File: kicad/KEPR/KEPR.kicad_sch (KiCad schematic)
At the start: 0 parts

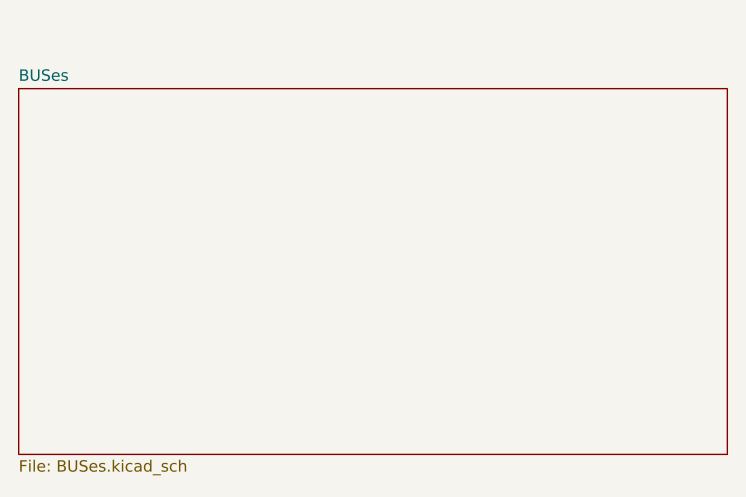
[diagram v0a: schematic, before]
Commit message: Definido os demais buses, criado folha do carimbo, versão 0.5
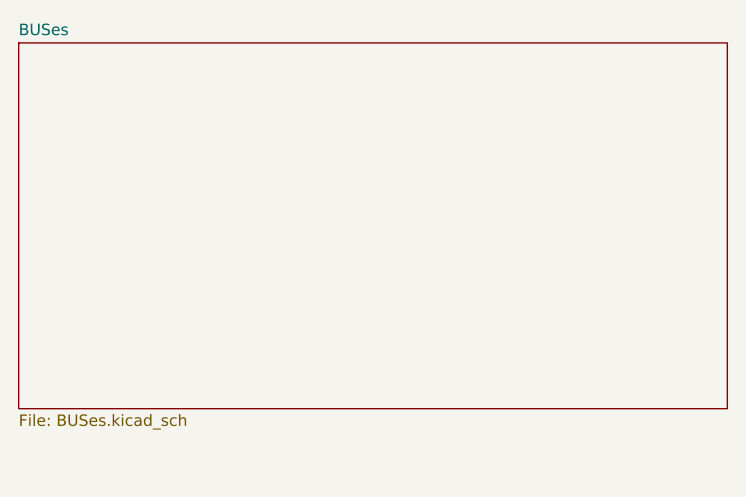
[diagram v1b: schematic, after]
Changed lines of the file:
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@@
 	)
 	(sheet
-		(at 30.48 25.4)
+		(at 30.48 20.32)
 		(size 78.74 40.64)
 		(exclude_from_sim no)
@@
 		)
 		(fill
-			(color 0 0 0 0.0000)
+			(color 255 97 121 1.0000)
 		)
 		(property "Sheetname" "BUSes"
-			(at 30.48 24.6884 0)
+			(at 30.48 19.6084 0)
 			(effects
 				(font
@@
 		)
 		(property "Sheetfile" "BUSes.kicad_sch"
-			(at 30.48 66.6246 0)
+			(at 30.48 61.5446 0)
 			(effects
 				(font
@@
 			(project "KEPR"
 				(path "/5d9e1dfb-5ec5-4e06-bbdb-9cbfa1c0b9f1"
-					(page "5")
+					(page "A001")
 				)
 			)

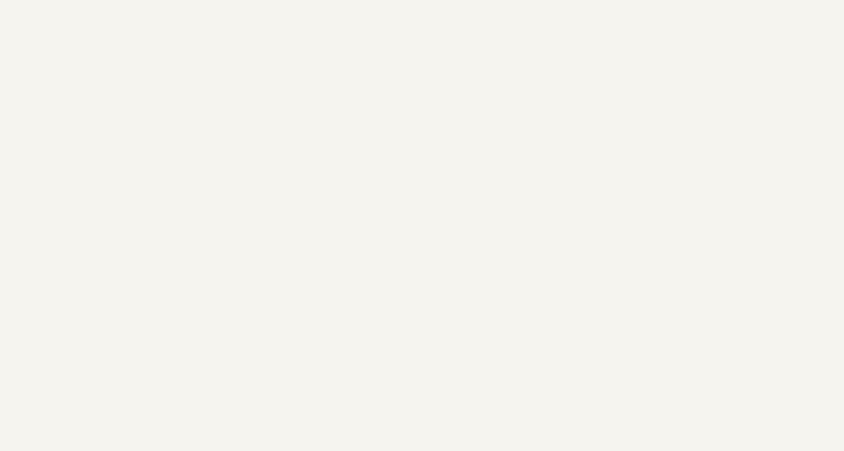
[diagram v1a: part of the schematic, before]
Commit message: Vários ajuste, sendo o mais importante a adição do power rail e iniciado o Wireless module
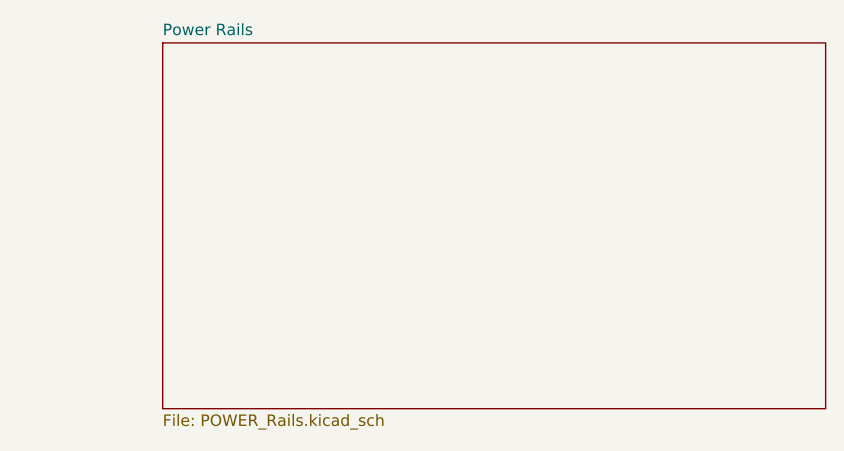
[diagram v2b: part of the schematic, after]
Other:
- added sheet Power Rails (POWER_Rails.kicad_sch)

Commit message: Diversos ajustes no Power Rail
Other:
- sheet Power Rails renamed Power
- added sheet UCE board (UCE_board.kicad_sch)
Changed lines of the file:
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@@
 			(color 0 0 0 0.0000)
 		)
-		(property "Sheetname" "Power Rails"
+		(property "Sheetname" "Power"
 			(at 137.16 19.6084 0)
 			(effects
@@
 			(project "KEPR"
 				(path "/5d9e1dfb-5ec5-4e06-bbdb-9cbfa1c0b9f1"
-					(page "A001")
+					(page "A002")
 				)
 			)
+		)
+	)
+	(sheet
+		(at 238.76 20.32)
+		(size 81.28 40.64)
+		(exclude_from_sim no)
+		(in_bom yes)
+		(on_board yes)
+		(dnp no)
+		(fields_autoplaced yes)
+		(stroke
+			(width 0.1524)
+			(type solid)
+		)
+		(fill
+			(color 255 23 51 1.0000)
+		)
+		(property "Sheetname" "UCE board"
+			(at 238.76 19.6084 0)
+			(effects
+				(font
+					(size 1.27 1.27)
+				)
+				(justify left bottom)
+			)
+		)
+		(property "Sheetfile" "UCE_board.kicad_sch"
+			(at 238.76 61.5446 0)
+			(effects
+				(font
+					(size 1.27 1.27)
+				)
+				(justify left top)
+			)
+		)
+		(instances
+			(project "KEPR"
+				(path "/5d9e1dfb-5ec5-4e06-bbdb-9cbfa1c0b9f1"
+					(page "A003")
+				)
+			)
